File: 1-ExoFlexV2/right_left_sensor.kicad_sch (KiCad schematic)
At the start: 17 parts, among them J92 Jumper, J93 Jumper, U51 Inverter, U52 Inverter, U53 AND Gate, U54 Inverter, U55 Inverter, U56 AND Gate, U57 OR Gate

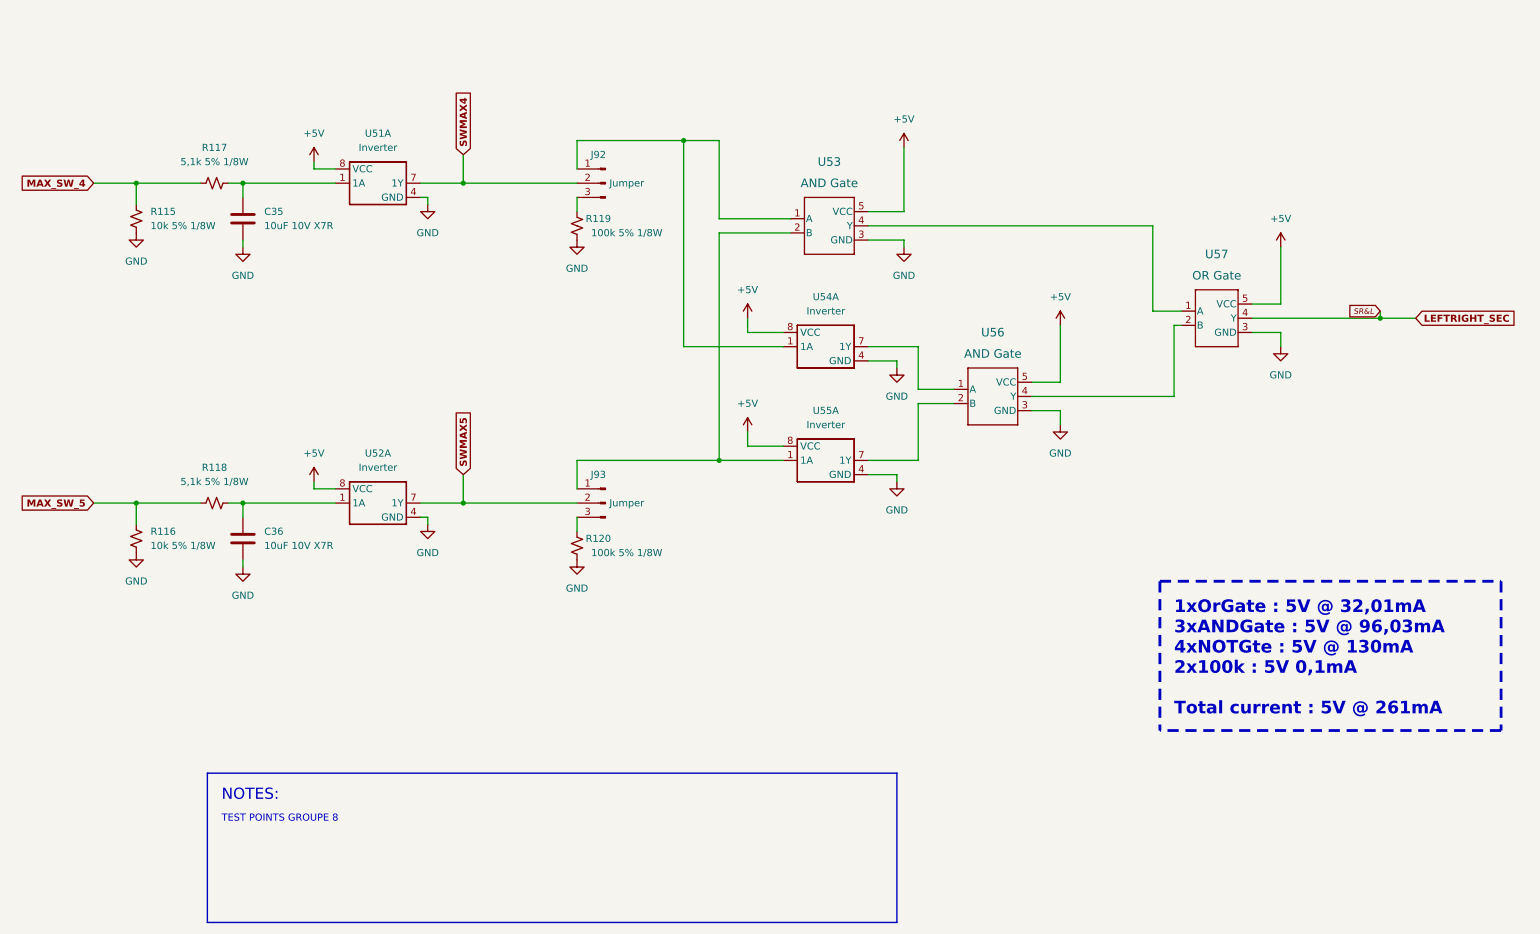
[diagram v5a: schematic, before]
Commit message: Finalisation 3
- Changement des régulateur de tension
- Retrait de test point inutile
- Changement de jumper mal positionner
- Ajout de Mounting holes et fiducial
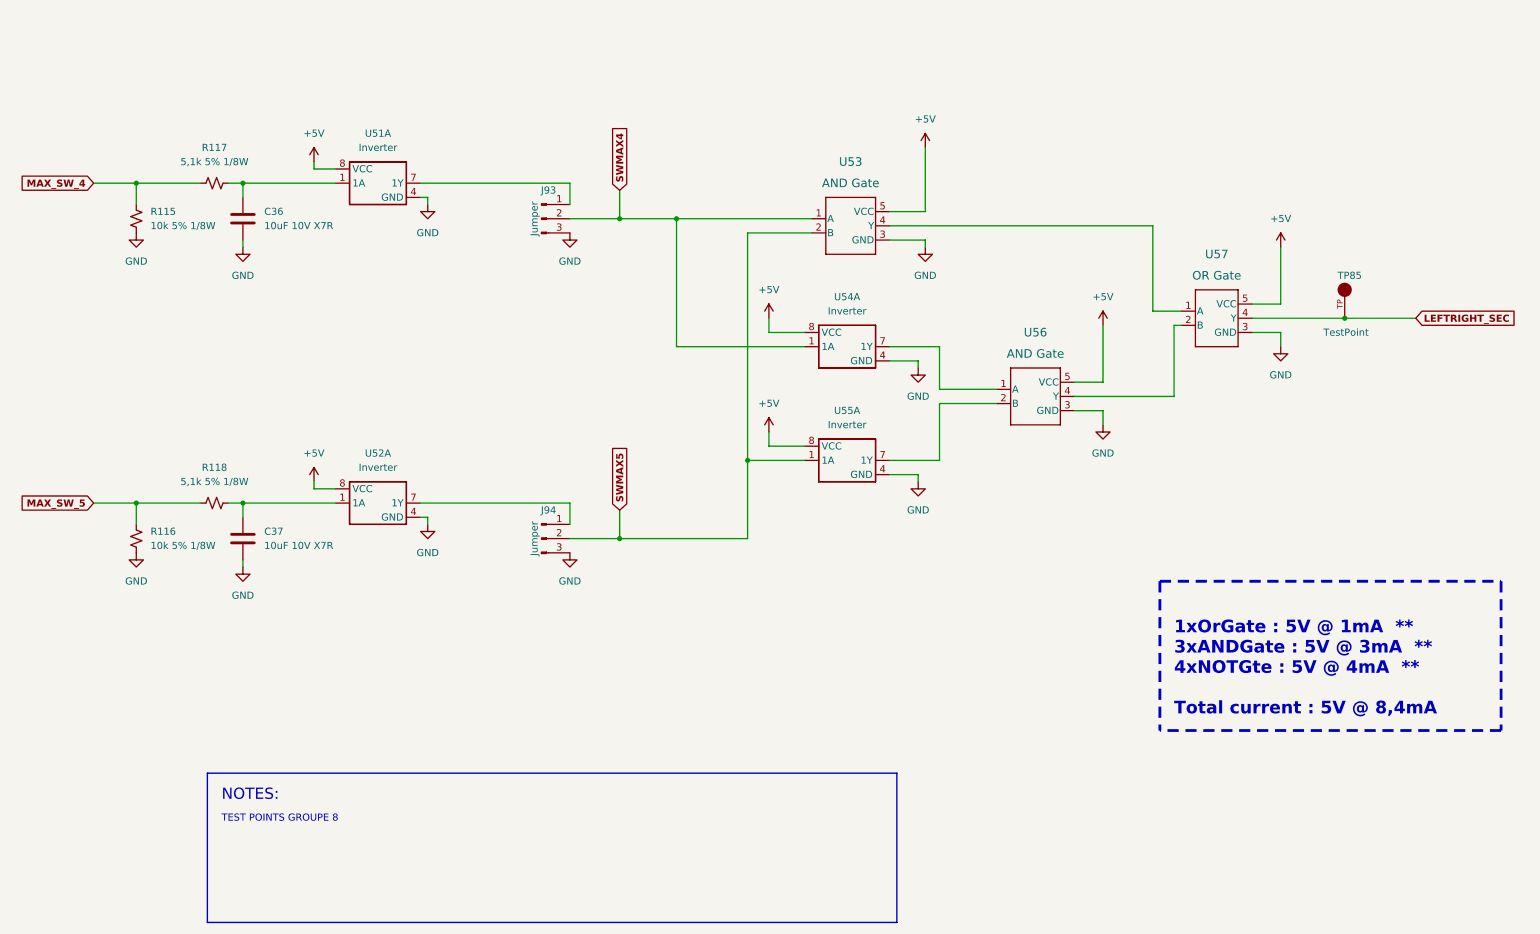
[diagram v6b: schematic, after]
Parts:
- removed R119, R120: 100k 5% 1/8W, Resistor_SMD:R_0805_2012Metric, symbol Device:R_Small_US
- added TP85: TestPoint, FootPrint:KEYSTONE_5005, symbol SymLib:5005
- J93: renamed from J92; footprint Connector_PinSocket_2.54mm:PinSocket_1x03_P2.54mm_Vertical -> Connector_PinHeader_2.54mm:PinHeader_1x03_P2.54mm_Vertical
- J94: renamed from J93; footprint Connector_PinSocket_2.54mm:PinSocket_1x03_P2.54mm_Vertical -> Connector_PinHeader_2.54mm:PinHeader_1x03_P2.54mm_Vertical
- renumbered C35 to C36, C36 to C37
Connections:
- net GND: now also J93.3 (Pin_3), J94.3 (Pin_3)
- net LEFTRIGHT_SEC: now also TP85.TP
- net SWMAX4: now also U53.1 (A), U54.1 (1A); no longer U51.7 (1Y)
- net SWMAX5: now also U53.2 (B), U55.1 (1A); no longer U52.7 (1Y)
- new net: J93.1 (Pin_1), U51.7 (1Y)
- new net: J94.1 (Pin_1), U52.7 (1Y)
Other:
- note added: "1xOrGate : 5V @ 1mA ** 3xANDGate : 5V @ 3mA ** 4xNOTGte : 5V @ 4mA ** Total current : 5V @ 8,4mA"
- note removed: "1xOrGate : 5V @ 32,01mA 3xANDGate : 5V @ 96,03mA 4xNOTGte : 5V @ 130mA 2x100k : 5V 0,1mA Total current : 5V @ 261mA"
- moved on the sheet: J93, J94, U53, U54A, U55A, U56

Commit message: Finalisation schéma FIN
- Changement des uméro pour les inverseurs
- Changement des connecteur et début de placement
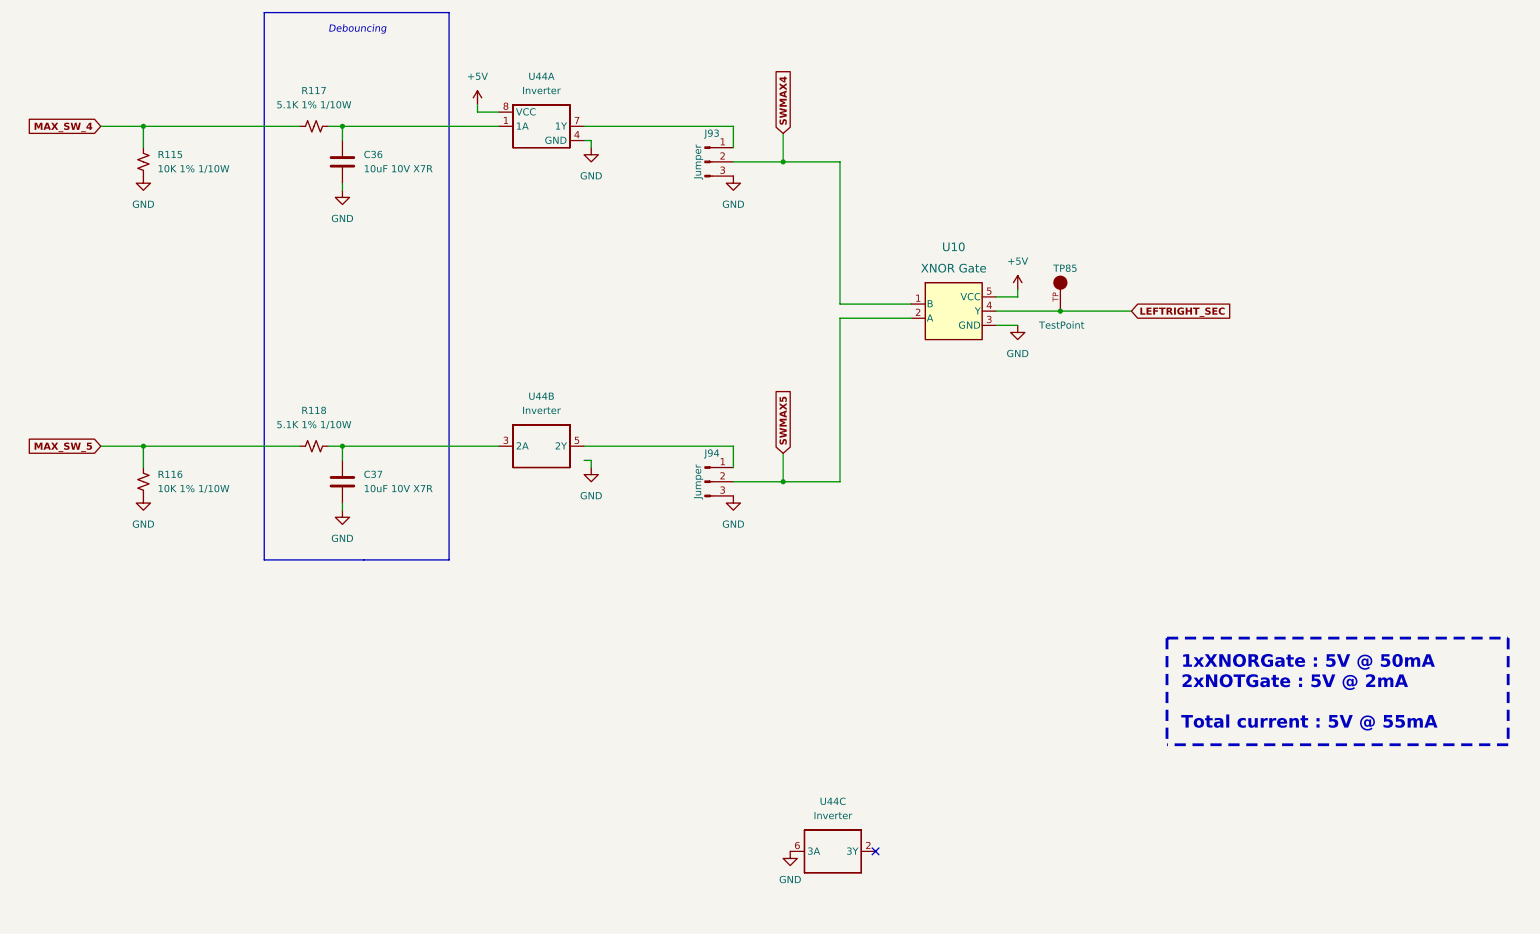
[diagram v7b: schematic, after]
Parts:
- removed U51, U52, U54, U55: Inverter, FootPrint:SN74LVC3G14DCUT, symbol SymLib:SN74LVC3G14DCUT_V2
- removed U53, U56: AND Gate, FootPrint:SOT95P270X145-5N, symbol SymLib:SN74LVC1G08DBVR
- removed U57: OR Gate, FootPrint:SOT95P270X145-5N, symbol SymLib:SN74LVC1G32DBVR
- added U10: XNOR Gate, FootPrintLib:SC-74A_SOT753_NEX, symbol SymLib:74LV1T87GVH
- added U44: Inverter, FootPrint:SN74LVC3G14DCUT, symbol SymLib:SN74LVC3G14DCUT_V2
- R115, R116: value 10k 5% 1/8W -> 10K 1% 1/10W; footprint Resistor_SMD:R_0805_2012Metric -> Resistor_SMD:R_0603_1608Metric; DESCRIPTION 10 kOhms ±5% 0.125W, 1/8W Chip Resistor 0805 (2012 Metric) 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 -> 10 kOhms ±1% 0.1W, 1/10W Chip Resistor 0603 (1608 Metric) A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; PACKAGE 0805 (2012 Metric) -> 0603 (1608 Metric); PART NUMBER ERJ-6GEYJ103V -> ERJ-3EKF1002V
- R117, R118: value 5,1k 5% 1/8W -> 5.1K 1% 1/10W; footprint Resistor_SMD:R_0805_2012Metric -> Resistor_SMD:R_0603_1608Metric; DESCRIPTION 5.1 kOhms ±5% 0.125W, 1/8W Chip Resistor 0805 (2012 Metric)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 -> 5.1 kOhms ±1% 0.1W, 1/10W Chip Resistor 0603 (1608 Metric) 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; PACKAGE 0805 (2012 Metric) -> 0603 (1608 Metric); PART NUMBER ERJ-6GEYJ512V -> ERJ-3EKF5101V
- TP85: NOTES (none) -> DO NOT POPULATE; PURCHASE-URL https://pricing.snapeda.com/search/part/5005/?ref=eda -> (none)
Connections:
- net +5V: now also U10.5 (VCC), U44.8 (VCC)
- net GND: now also U10.3 (GND), U44.4 (GND), U44.6 (3A)
- net LEFTRIGHT_SEC: now also U10.4 (Y)
- net SWMAX4: now also U10.1 (B)
- net SWMAX5: now also U10.2 (A)
- net at C37.1, R118.2: now also U44.3 (2A)
- net at C36.1, R117.2: now also U44.1 (1A)
- net at J93.1 (Pin_1): now also U44.7 (1Y)
- net at J94.1 (Pin_1): now also U44.5 (2Y)
- no-connect marks 0 -> 1
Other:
- note added: "1xXNORGate : 5V @ 50mA 2xNOTGate : 5V @ 2mA Total current : 5V @ 55mA"
- note added: "Debouncing"
- note removed: "1xOrGate : 5V @ 1mA ** 3xANDGate : 5V @ 3mA ** 4xNOTGte : 5V @ 4mA ** Total current : 5V @ 8,4mA"
- note removed: "NOTES:"
- note removed: "TEST POINTS GROUPE 8"
- moved on the sheet: C36, C37, J93, J94, R115, R116, R117, R118, TP85

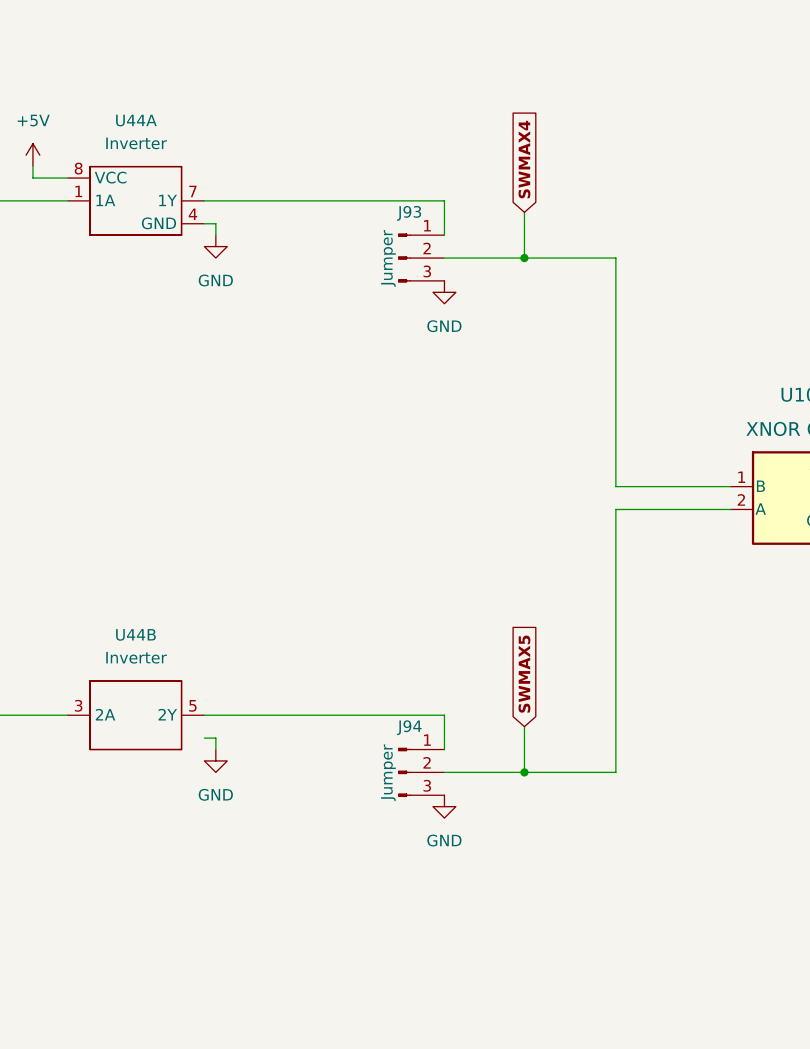
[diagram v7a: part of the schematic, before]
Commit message: Routage pour Review 1
- Replacement des test point pour faciliter le rework
- Correction des erreurs dans le BOM
-
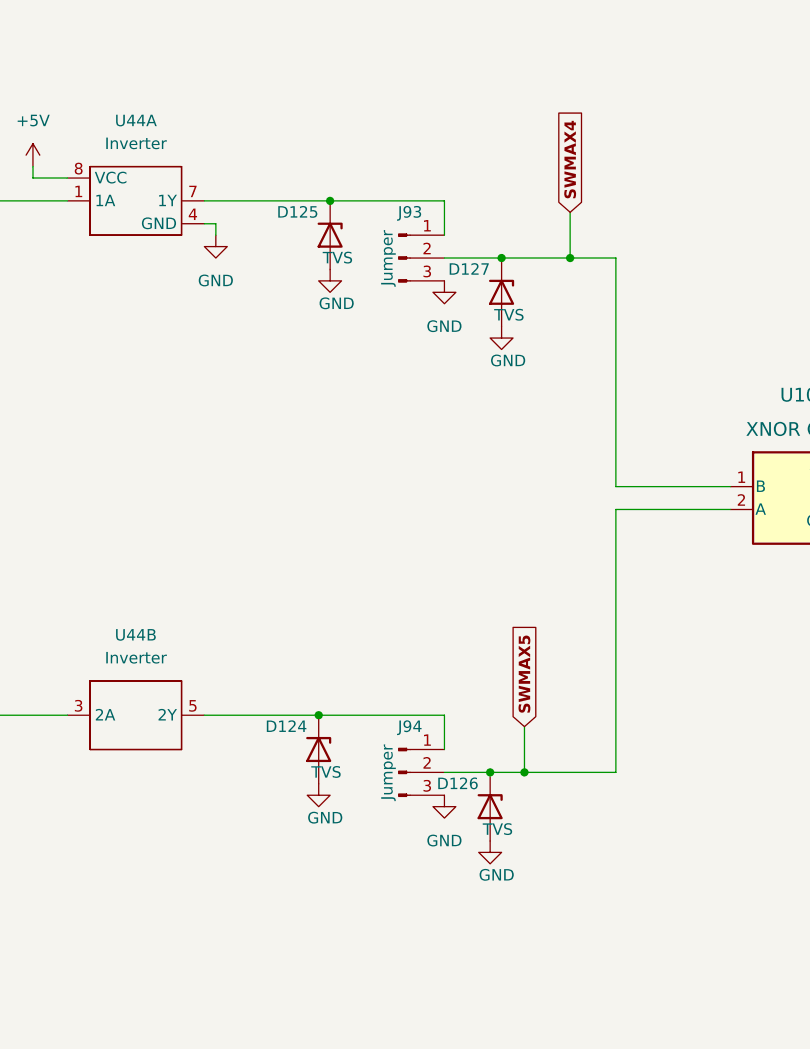
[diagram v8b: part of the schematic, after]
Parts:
- added D124, D125, D126, D127: TVS, FootPrint:DPY2_TEX, symbol Device:D_Zener
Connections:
- net GND: now also D124.2 (A), D125.2 (A), D126.2 (A), D127.2 (A)
- net SWMAX4: now also D127.1 (K)
- net SWMAX5: now also D126.1 (K)
- net at J94.1 (Pin_1), U44.5 (2Y): now also D124.1 (K)
- net at J93.1 (Pin_1), U44.7 (1Y): now also D125.1 (K)
